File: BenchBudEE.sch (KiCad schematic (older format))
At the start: 0 parts

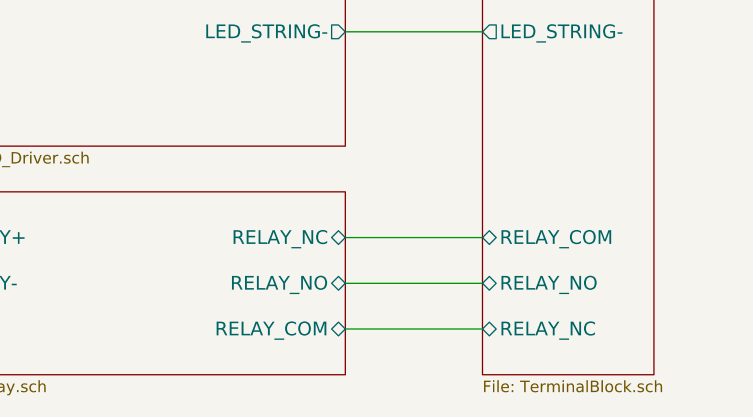
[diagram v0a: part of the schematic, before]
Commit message: Updates from Reality Check video
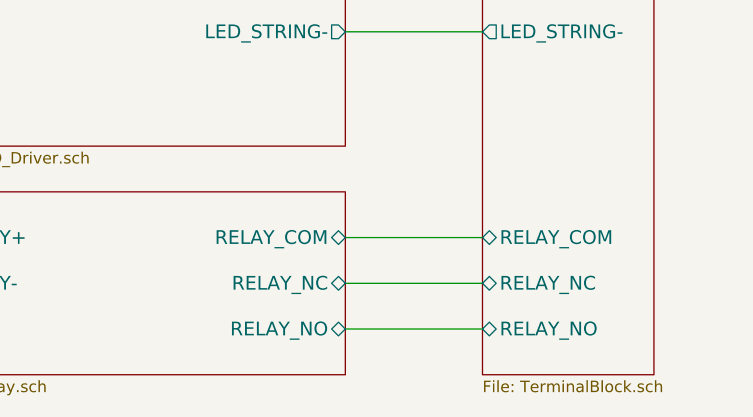
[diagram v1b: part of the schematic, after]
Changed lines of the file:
@@
 F0 "Relay" 50
 F1 "Relay.sch" 50
-F2 "RELAY_NC" B R 9400 5500 60
-F3 "RELAY_NO" B R 9400 5700 60
-F4 "RELAY_COM" B R 9400 5900 60
+F2 "RELAY_NC" B R 9400 5700 60
+F3 "RELAY_NO" B R 9400 5900 60
+F4 "RELAY_COM" B R 9400 5500 60
 F5 "RELAY+" I L 7600 5500 60
 F6 "RELAY-" O L 7600 5700 60
@@
 F10 "TC_IN-" I L 10000 3500 60
 F11 "RELAY_COM" B L 10000 5500 60
-F12 "RELAY_NO" B L 10000 5700 60
-F13 "RELAY_NC" B L 10000 5900 60
+F12 "RELAY_NO" B L 10000 5900 60
+F13 "RELAY_NC" B L 10000 5700 60
 $EndSheet
 $Sheet
